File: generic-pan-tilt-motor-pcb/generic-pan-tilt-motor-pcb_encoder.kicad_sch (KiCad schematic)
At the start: 11 parts, among them U3 74LVC3G17

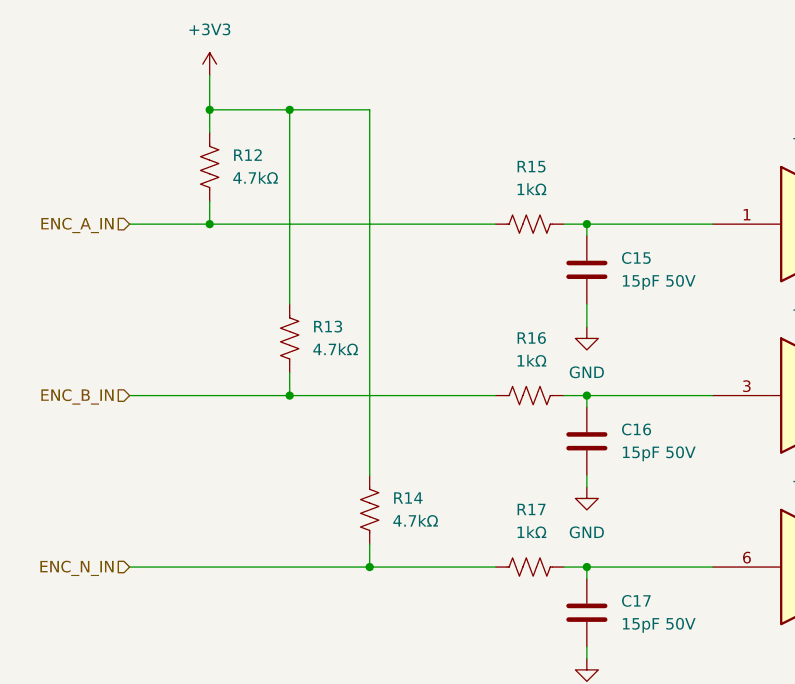
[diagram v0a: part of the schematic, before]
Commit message: motor pcb all footprints, ov circuit
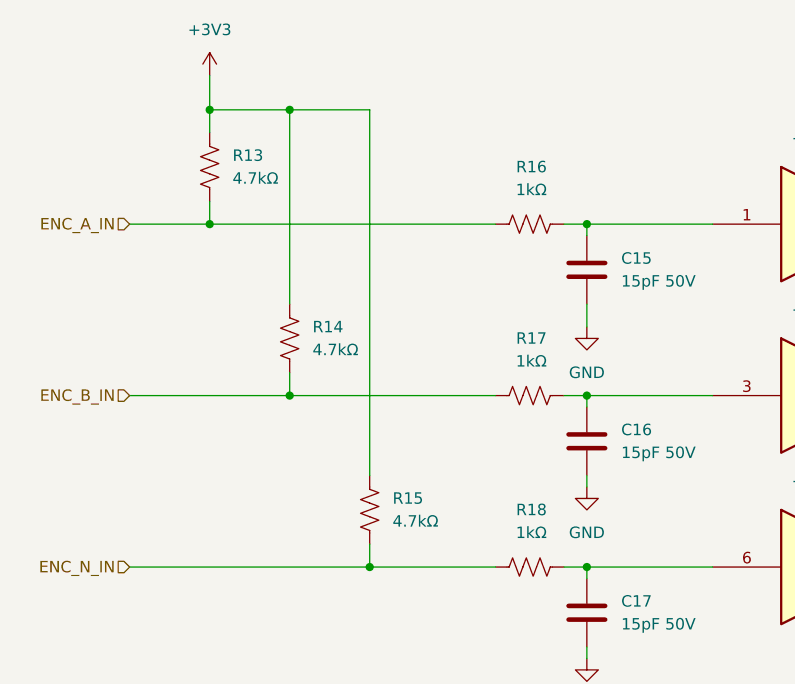
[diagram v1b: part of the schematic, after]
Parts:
- C15, C16, C17: footprint (none) -> Capacitor_SMD:C_0603_1608Metric
- C18: footprint (none) -> Capacitor_SMD:C_0402_1005Metric
- R13: renamed from R12; footprint (none) -> Resistor_SMD:R_0402_1005Metric
- R14: renamed from R13; footprint (none) -> Resistor_SMD:R_0402_1005Metric
- R15: renamed from R14; footprint (none) -> Resistor_SMD:R_0402_1005Metric
- R16: renamed from R15; footprint (none) -> Resistor_SMD:R_0402_1005Metric
- R17: renamed from R16; footprint (none) -> Resistor_SMD:R_0402_1005Metric
- R18: renamed from R17; footprint (none) -> Resistor_SMD:R_0402_1005Metric
- U3: footprint (none) -> Package_SO:VSSOP-8_2.3x2mm_P0.5mm; digikey# (none) -> 296-18818-1-ND; manf# (none) -> SN74LVC3G17DCUR; mouser# (none) -> 595-SN74LVC3G17DCUR

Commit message: motor basic layout
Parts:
- C22: renamed from C18; value 0.1µF 10V -> 0.1µF 16V
- renumbered C15 to C19, C16 to C20, C17 to C21
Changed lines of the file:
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@@
 		(dnp no)
 		(fields_autoplaced yes)
-		(property "Reference" "#PWR046"
+		(property "Reference" "#PWR050"
 			(at 198.12 104.14 0)
 			(effects
@@
 			(project "generic-pan-tilt-motor-pcb"
 				(path "/bfc49584-1093-4a5f-ad88-bc47ac53d02e/d2c76bbf-2b51-4e74-a87d-8fabba51c107"
-					(reference "#PWR046")
+					(reference "#PWR050")
 					(unit 1)
 				)
@@
 		(dnp no)
 		(fields_autoplaced yes)
-		(property "Reference" "#PWR041"
+		(property "Reference" "#PWR045"
 			(at 78.74 71.12 0)
 			(effects
@@
 			(project "generic-pan-tilt-motor-pcb"
 				(path "/bfc49584-1093-4a5f-ad88-bc47ac53d02e/d2c76bbf-2b51-4e74-a87d-8fabba51c107"
-					(reference "#PWR041")
+					(reference "#PWR045")
 					(unit 1)
 				)
@@
 		(dnp no)
 		(fields_autoplaced yes)
-		(property "Reference" "C16"
+		(property "Reference" "C20"
 			(at 124.46 106.6799 0)
 			(effects
@@
 			(project "generic-pan-tilt-motor-pcb"
 				(path "/bfc49584-1093-4a5f-ad88-bc47ac53d02e/d2c76bbf-2b51-4e74-a87d-8fabba51c107"
-					(reference "C16")
+					(reference "C20")
 					(unit 1)
 				)
@@
 		(dnp no)
 		(fields_autoplaced yes)
-		(property "Reference" "#PWR045"
+		(property "Reference" "#PWR049"
 			(at 198.12 90.17 0)
 			(effects
@@
 			(project "generic-pan-tilt-motor-pcb"
 				(path "/bfc49584-1093-4a5f-ad88-bc47ac53d02e/d2c76bbf-2b51-4e74-a87d-8fabba51c107"
-					(reference "#PWR045")
+					(reference "#PWR049")
 					(unit 1)
 				)
@@
 		(dnp no)
 		(fields_autoplaced yes)
-		(property "Reference" "#PWR047"
+		(property "Reference" "#PWR051"
 			(at 218.44 120.65 0)
 			(effects
@@
 			(project "generic-pan-tilt-motor-pcb"
 				(path "/bfc49584-1093-4a5f-ad88-bc47ac53d02e/d2c76bbf-2b51-4e74-a87d-8fabba51c107"
-					(reference "#PWR047")
+					(reference "#PWR051")
 					(unit 1)
 				)
@@
 		(dnp no)
 		(fields_autoplaced yes)
-		(property "Reference" "#PWR044"
+		(property "Reference" "#PWR048"
 			(at 120.65 138.43 0)
 			(effects
@@
 			(project "generic-pan-tilt-motor-pcb"
 				(path "/bfc49584-1093-4a5f-ad88-bc47ac53d02e/d2c76bbf-2b51-4e74-a87d-8fabba51c107"
-					(reference "#PWR044")
+					(reference "#PWR048")
 					(unit 1)
 				)
@@
 		(dnp no)
 		(fields_autoplaced yes)
-		(property "Reference" "C17"
+		(property "Reference" "C21"
 			(at 124.46 125.7299 0)
 			(effects
@@
 			(project "generic-pan-tilt-motor-pcb"
 				(path "/bfc49584-1093-4a5f-ad88-bc47ac53d02e/d2c76bbf-2b51-4e74-a87d-8fabba51c107"
-					(reference "C17")
+					(reference "C21")
 					(unit 1)
 				)
@@
 		(dnp no)
 		(fields_autoplaced yes)
-		(property "Reference" "C15"
+		(property "Reference" "C19"
 			(at 124.46 87.6299 0)
 			(effects
@@
 			(project "generic-pan-tilt-motor-pcb"
 				(path "/bfc49584-1093-4a5f-ad88-bc47ac53d02e/d2c76bbf-2b51-4e74-a87d-8fabba51c107"
-					(reference "C15")
+					(reference "C19")
 					(unit 1)
 				)
@@
 		(dnp no)
 		(fields_autoplaced yes)
-		(property "Reference" "#PWR042"
+		(property "Reference" "#PWR046"
 			(at 120.65 101.6 0)
 			(effects
@@
 			(project "generic-pan-tilt-motor-pcb"
 				(path "/bfc49584-1093-4a5f-ad88-bc47ac53d02e/d2c76bbf-2b51-4e74-a87d-8fabba51c107"
-					(reference "#PWR042")
+					(reference "#PWR046")
 					(unit 1)
 				)
@@
 		(dnp no)
 		(fields_autoplaced yes)
-		(property "Reference" "#PWR043"
+		(property "Reference" "#PWR047"
 			(at 120.65 119.38 0)
 			(effects
@@
 			(project "generic-pan-tilt-motor-pcb"
 				(path "/bfc49584-1093-4a5f-ad88-bc47ac53d02e/d2c76bbf-2b51-4e74-a87d-8fabba51c107"
-					(reference "#PWR043")
+					(reference "#PWR047")
 					(unit 1)
 				)
@@
 		(on_board yes)
 		(dnp no)
-		(property "Reference" "C18"
+		(property "Reference" "C22"
 			(at 201.93 91.4399 0)
 			(effects
@@
 			)
 		)
-		(property "Value" "0.1µF 10V"
+		(property "Value" "0.1µF 16V"
 			(at 201.93 93.9799 0)
 			(effects
@@
 			(project "generic-pan-tilt-motor-pcb"
 				(path "/bfc49584-1093-4a5f-ad88-bc47ac53d02e/d2c76bbf-2b51-4e74-a87d-8fabba51c107"
-					(reference "C18")
-					(unit 1)
-				)
+					(reference "C22")
+					(unit 1)
+				)

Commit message: motor pcb layout up to enc filter
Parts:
- C22: footprint Capacitor_SMD:C_0402_1005Metric -> Capacitor_SMD:C_0603_1608Metric
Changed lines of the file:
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@@
 			)
 		)
-		(property "Footprint" "Capacitor_SMD:C_0402_1005Metric"
+		(property "Footprint" "Capacitor_SMD:C_0603_1608Metric"
 			(at 199.0852 96.52 0)
 			(effects

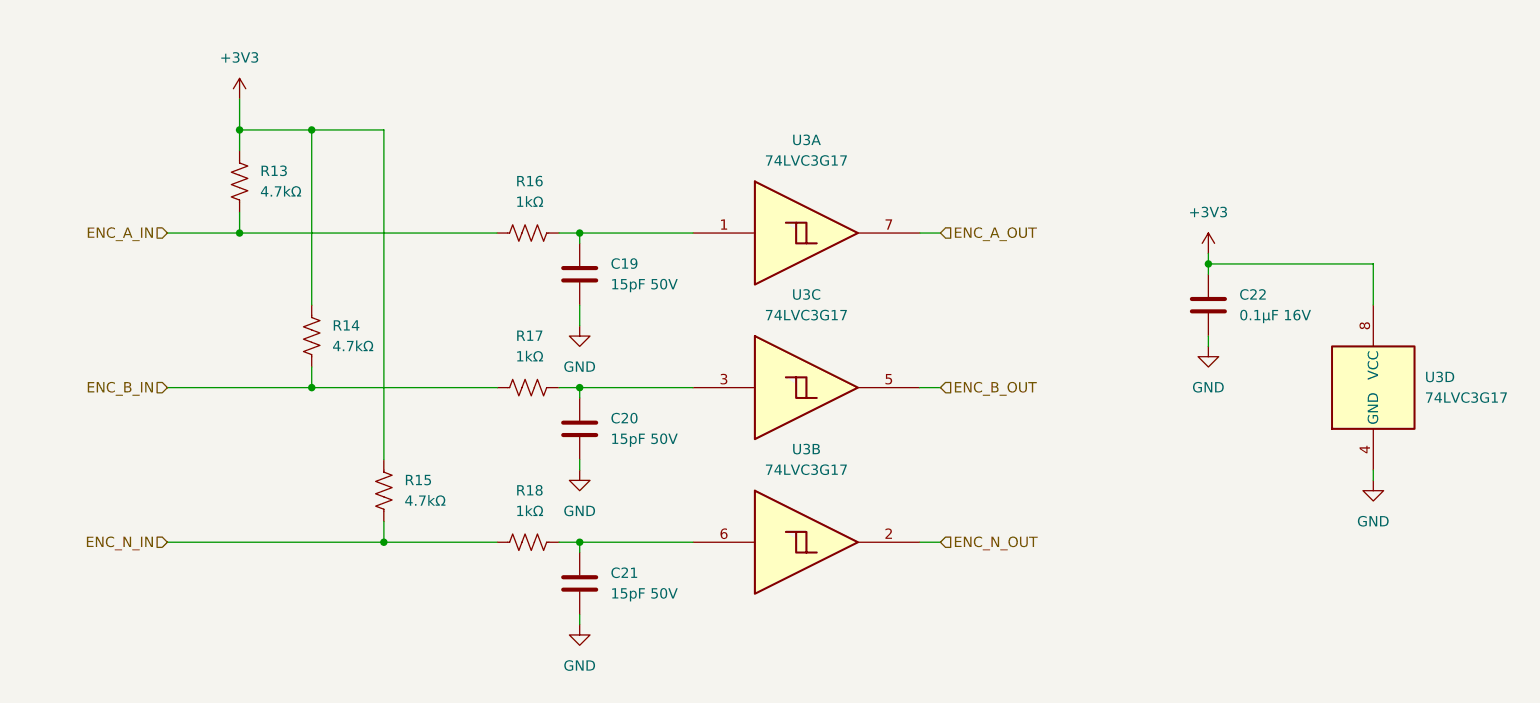
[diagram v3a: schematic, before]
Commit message: fix part numbers, add newark parts, separate fields for part desc
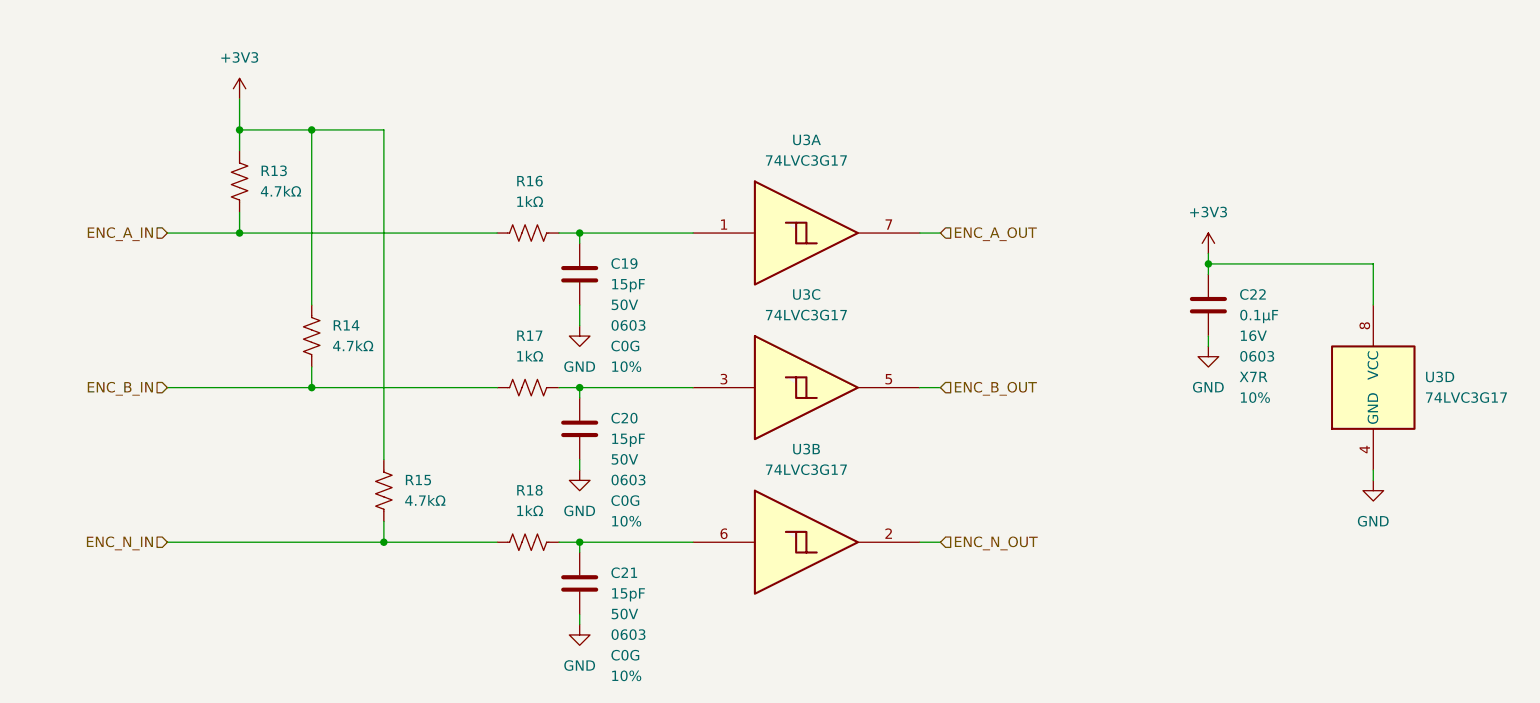
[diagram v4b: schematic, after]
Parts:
- C19, C20, C21: value 15pF 50V -> 15pF; Case Code (none) -> 0603; Dielectric (none) -> C0G; Tolerance (none) -> 10%; Voltage (none) -> 50V; manf# (none) -> CC0603KRNPO9BN150; mouser# (none) -> 603­-CC603KRNPO9BN150
- C22: value 0.1µF 16V -> 0.1µF; Case Code (none) -> 0603; Dielectric (none) -> X7R; Tolerance (none) -> 10%; Voltage (none) -> 16V; manf# (none) -> CL10B104KO8NFNC; mouser# (none) -> 187-CL10B104KO8NFNC
- U3: newark# (none) -> 29AH7645

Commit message: motor fix flipped spi mcp, spi tristate for drc, silk screw terminals, all parts manf and vendors
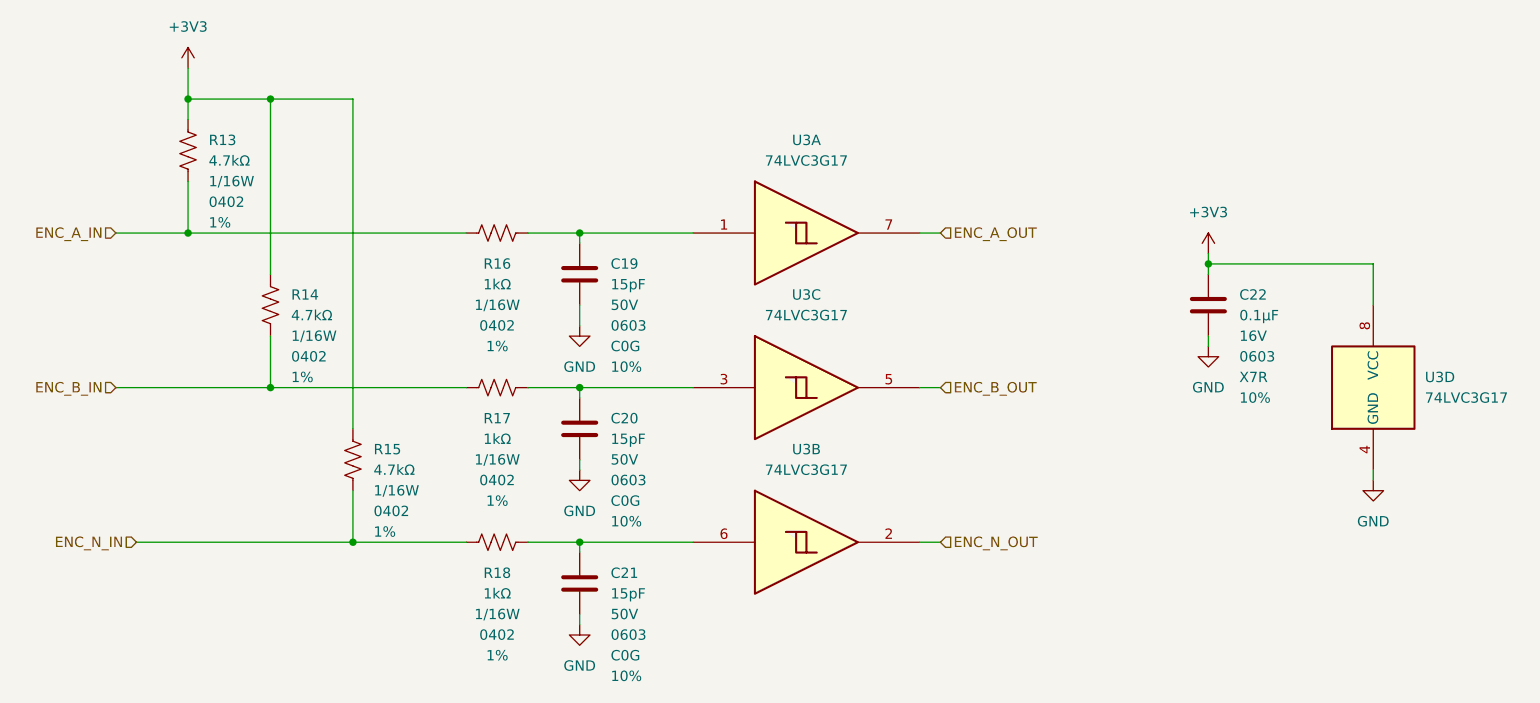
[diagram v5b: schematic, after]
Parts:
- C19, C20, C21: digikey# (none) -> 311-4028-1-ND; lcsc# (none) -> C2173971; newark# (none) -> 83AK0180
- C22: digikey# (none) -> 1276-1005-1-ND; lcsc# (none) -> C66501; manf# CL10B104KO8NFNC -> CL10B104KO8NNNC; mouser# 187-CL10B104KO8NFNC -> 187-CL10B104KO8NNNC; newark# (none) -> 82AC9325
- R13, R14, R15: Case Code (none) -> 0402; Power (none) -> 1/16W; Tolerance (none) -> 1%; digikey# (none) -> CR0402-FX-4701GLFCT-ND; lcsc# (none) -> C2076851; manf# (none) -> CR0402-FX-4701GLF; mouser# (none) -> 652-CR0402FX-4701GLF; newark# (none) -> 34AK1324
- R16, R17, R18: Case Code (none) -> 0402; Power (none) -> 1/16W; Tolerance (none) -> 1%; digikey# (none) -> CR0402-FX-1001GLFCT-ND; lcsc# (none) -> C202394; manf# (none) -> CR0402-FX-1001GLF; mouser# (none) -> 652-CR0402FX-1001GLF; newark# (none) -> 02J1761
- U3: lcsc# (none) -> C68245
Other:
- moved on the sheet: R15

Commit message: motor board fix fields, add drc exclusion
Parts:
- R13, R14, R15: mouser# 652-CR0402FX-4701GLF -> 652-CR0402FX-4701GLF
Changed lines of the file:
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@@
 			)
 		)
-		(property "mouser#" "652-CR0402FX-4701GLF "
+		(property "mouser#" "652-CR0402FX-4701GLF"
 			(at 72.39 73.66 0)
 			(effects
@@
 			)
 		)
-		(property "mouser#" "652-CR0402FX-4701GLF "
+		(property "mouser#" "652-CR0402FX-4701GLF"
 			(at 82.55 92.71 0)
 			(effects
@@
 			)
 		)
-		(property "mouser#" "652-CR0402FX-4701GLF "
+		(property "mouser#" "652-CR0402FX-4701GLF"
 			(at 92.71 111.76 0)
 			(effects
